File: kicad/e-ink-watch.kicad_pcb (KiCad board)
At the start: 4 copper layers, 40 x 40 mm, 45 parts, among them Q1 DMG2305UX, SW1 BTN1, SW2 BTN2, SW3 BTN3, U1 MDBT50Q-1MV2, U2 BQ25619, U3 MCP1700-3302

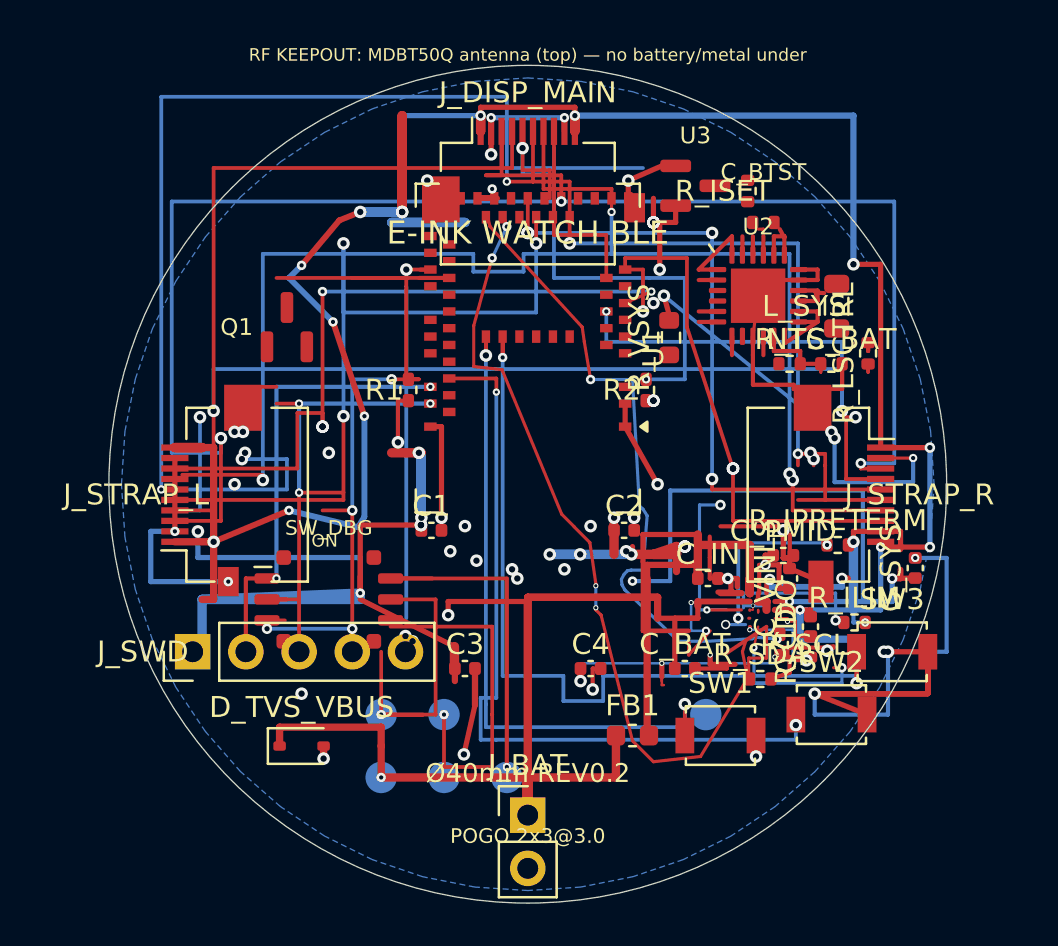
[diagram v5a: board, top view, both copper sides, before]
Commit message: Pass-BH: route VSYS, PSEL, and the display switch.
Unconnected drops from 22 to 17 with shorting_items still 0. The REGN path that failed clearance was not kept.

Co-authored-by: illiapliukhin <illiapliukhin@users.noreply.github.com>
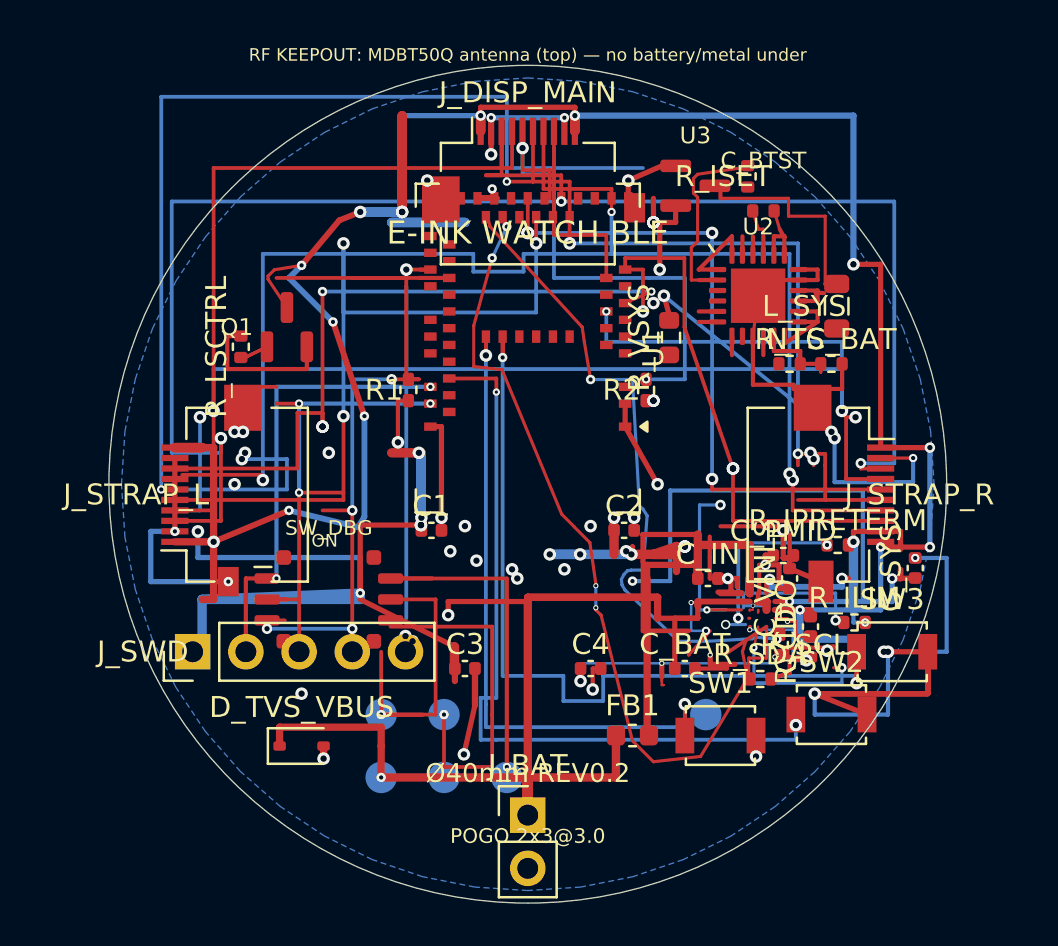
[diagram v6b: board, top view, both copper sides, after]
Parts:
- moved R_LSCTRL 30.0 mm to (86.3, 93.4)
- moved R_ISET 0.70 mm to (110.5, 85.3)
- moved C_BTST 0.55 mm to (111.2, 87.0)
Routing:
- net VSYS: track 32.4 -> 42.6 mm
- net PSEL: track 0.90 -> 9.01 mm
- net 3V3: track 105.3 -> 111.1 mm
- net 3V3_DISP: track 129.5 -> 133.0 mm
- net DISP_EN: track 0.80 -> 2.33 mm
- net BTST: track 1.48 -> 2.39 mm
- net SW: track 8.10 -> 9.01 mm
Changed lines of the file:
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@@
 	(footprint "R_0402_1005Metric"
 		(layer "F.Cu")
-		(at 110.5 86 90)
+		(at 110.5 85.3 90)
 		(descr "Resistor SMD 0402 (1005 Metric), square (rectangular) end terminal, IPC-7351 nominal, (Body size source: IPC-SM-782 page 72, https://www.pcb-3d.com/wordpress/wp-content/uploads/ipc-sm-782a_amendment_1_and_2.pdf), generated with kicad-footprint-generator")
 		(tags "resistor")
@@
 	(footprint "R_0402_1005Metric"
 		(layer "F.Cu")
-		(at 116.25 93.75 90)
+		(at 86.3 93.438 90)
 		(descr "Resistor SMD 0402 (1005 Metric), square (rectangular) end terminal, IPC-7351 nominal, (Body size source: IPC-SM-782 page 72, https://www.pcb-3d.com/wordpress/wp-content/uploads/ipc-sm-782a_amendment_1_and_2.pdf), generated with kicad-footprint-generator")
 		(tags "resistor")
@@
 	(segment
 		(start 104.65 89.2)
-		(end 107.6 89.2)
+		(end 107.48 89.2)
 		(width 0.18)
 		(layer "F.Cu")
@@
 	)
 	(segment
-		(start 107.6 89.2)
-		(end 107.6 92.5)
+		(start 107.48 89.2)
+		(end 107.48 92.5)
 		(width 0.18)
 		(layer "F.Cu")
@@
 	)
 	(segment
-		(start 107.6 92.5)
+		(start 107.48 92.5)
 		(end 109.8 99.25)
 		(width 0.18)
@@
 	(footprint "Resistor_SMD:R_0402_1005Metric"
 		(layer "F.Cu")
-		(at 111.25 87.5)
+		(at 111.25 86.95)
 		(descr "47nF")
 		(property "Reference" "C_BTST"
@@
 	)
 	(segment
-		(start 116.25 94.26)
-		(end 116.25 94.66)
+		(start 86.5 93.948)
+		(end 87.55 93.438)
 		(width 0.15)
 		(layer "F.Cu")
@@
 	)
 	(segment
-		(start 116.25 94.66)
-		(end 116.25 94.26)
+		(start 86.5 93.948)
+		(end 87.55 93.438)
 		(width 0.15)
 		(layer "F.Cu")
@@
 	)
 	(segment
-		(start 116.25 93.24)
-		(end 116.25 93.64)
+		(start 86.2 92.928)
+		(end 85.65 92.928)
 		(width 0.2)
 		(layer "F.Cu")
@@
 	)
 	(segment
-		(start 116.25 93.64)
-		(end 116.25 93.24)
+		(start 85.65 92.928)
+		(end 85.65 94.5)
 		(width 0.2)
 		(layer "F.Cu")
@@
 		(net 4)
 	)
+	(segment
+		(start 109.2 85.75)
+		(end 109.2 86.35)
+		(width 0.2)
+		(layer "F.Cu")
+		(net 5)
+	)
+	(segment
+		(start 109.2 86.35)
+		(end 112.45 86.35)
+		(width 0.15)
+		(layer "F.Cu")
+		(net 5)
+	)
+	(segment
+		(start 112.45 86.35)
+		(end 112.45 87.2)
+		(width 0.15)
+		(layer "F.Cu")
+		(net 5)
+	)
+	(segment
+		(start 112.45 87.2)
+		(end 114.2 87.2)
+		(width 0.15)
+		(layer "F.Cu")
+		(net 5)
+	)
+	(segment
+		(start 114.2 87.2)
+		(end 114.2 90.44)
+		(width 0.15)
+		(layer "F.Cu")
+		(net 5)
+	)
+	(segment
+		(start 114.2 90.44)
+		(end 114.75 90.438)
+		(width 0.2)
+		(layer "F.Cu")
+		(net 5)
+	)
+	(segment
+		(start 111.01 87.82)
+		(end 110.74 86.95)
+		(width 0.15)
+		(layer "F.Cu")
+		(net 40)
+	)
+	(segment
+		(start 112.03 87.82)
+		(end 111.76 86.95)
+		(width 0.15)
+		(layer "F.Cu")
+		(net 33)
+	)
+	(segment
+		(start 108.162 90.25)
+		(end 107.81 90.25)
+		(width 0.15)
+		(layer "F.Cu")
+		(net 39)
+	)
+	(segment
+		(start 107.81 90.25)
+		(end 107.81 88.7)
+		(width 0.15)
+		(layer "F.Cu")
+		(net 39)
+	)
+	(segment
+		(start 107.81 88.7)
+		(end 108.11 88.4)
+		(width 0.15)
+		(layer "F.Cu")
+		(net 39)
+	)
+	(segment
+		(start 108.11 88.4)
+		(end 108.11 86.3)
+		(width 0.15)
+		(layer "F.Cu")
+		(net 39)
+	)
+	(segment
+		(start 108.11 86.3)
+		(end 107.91 86.1)
+		(width 0.15)
+		(layer "F.Cu")
+		(net 39)
+	)
+	(segment
+		(start 107.91 86.1)
+		(end 107.91 85.4)
+		(width 0.15)
+		(layer "F.Cu")
+		(net 39)
+	)
+	(segment
+		(start 107.91 85.4)
+		(end 108.11 85.2)
+		(width 0.15)
+		(layer "F.Cu")
+		(net 39)
+	)
+	(segment
+		(start 108.11 85.2)
+		(end 110.5 84.85)
+		(width 0.15)
+		(layer "F.Cu")
+		(net 39)
+	)
+	(segment
+		(start 88.5 91.56)
+		(end 87.6 90.21)
+		(width 0.15)
+		(layer "F.Cu")
+		(net 3)
+	)
+	(segment
+		(start 87.6 90.21)
+		(end 87.6 90.06)
+		(width 0.15)
+		(layer "F.Cu")
+		(net 3)
+	)
+	(segment
+		(start 87.6 90.06)
+		(end 87.9 89.76)
+		(width 0.15)
+		(layer "F.Cu")
+		(net 3)
+	)
+	(segment
+		(start 87.9 89.76)
+		(end 89.2 89.55)
+		(width 0.15)
+		(layer "F.Cu")
+		(net 3)
+	)
+	(segment
+		(start 85.65 94.5)
+		(end 89.45 94.5)
+		(width 0.2)
+		(layer "F.Cu")
+		(net 2)
+	)
+	(segment
+		(start 89.45 94.5)
+		(end 89.45 93.8)
+		(width 0.2)
+		(layer "F.Cu")
+		(net 2)
+	)
 	(via

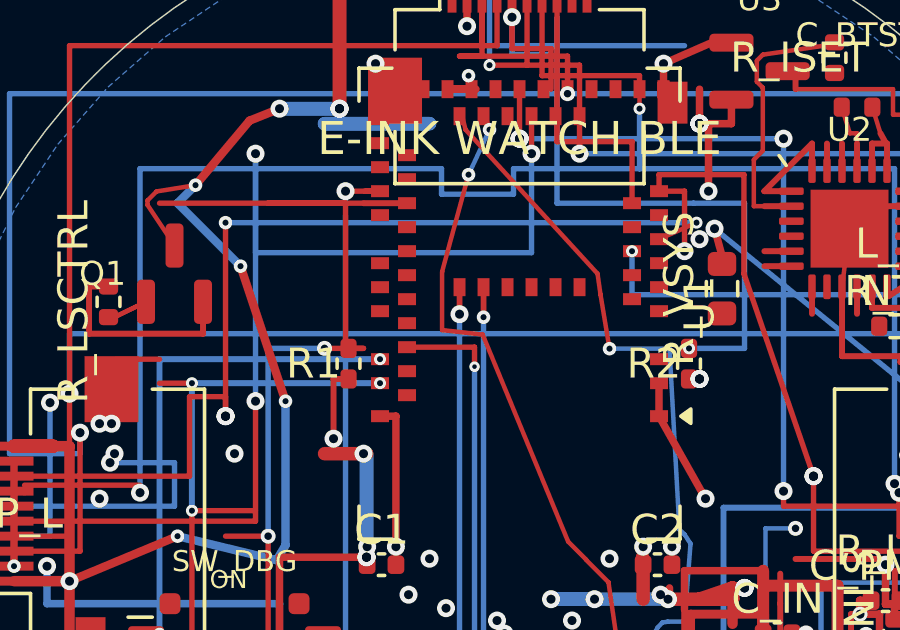
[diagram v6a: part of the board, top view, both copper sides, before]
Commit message: Pass-BI: join Q1 source to the module 3V3 rail.
Slide the EPD_BUSY_L via to (90.20, 90.96) so one 0.15 mm track fits under nRESET, and land that track on the module rail at (93.80, 96.30). shorting stays 0, unc 17 to 16.

Co-authored-by: illiapliukhin <illiapliukhin@users.noreply.github.com>
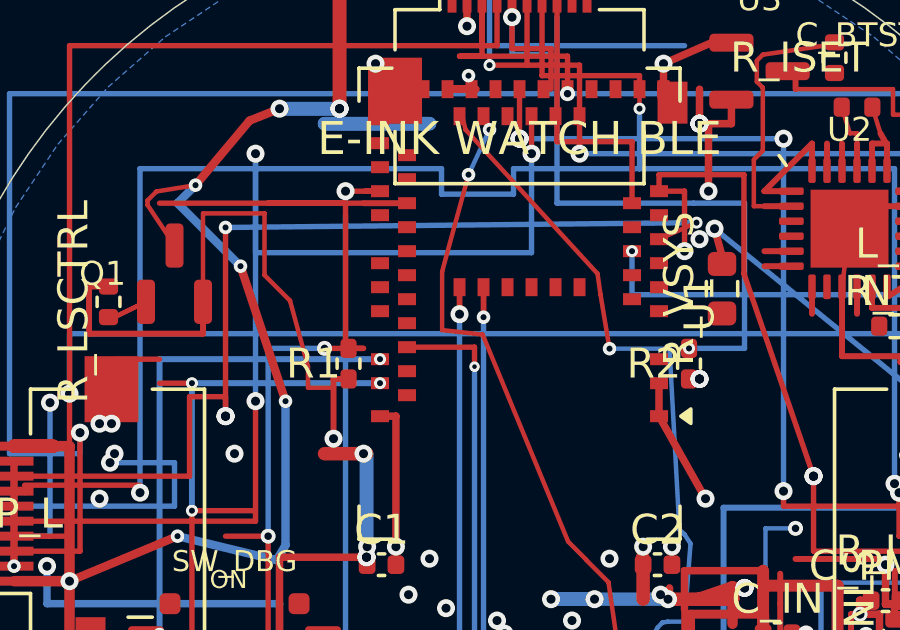
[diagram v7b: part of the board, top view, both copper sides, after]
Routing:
- net 3V3: track 111.1 -> 123.5 mm
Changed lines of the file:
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@@
 	(segment
 		(start 105.9 90.8)
-		(end 90.2 90.8)
+		(end 90.2 90.96)
 		(width 0.18)
 		(layer "B.Cu")
@@
 	)
 	(via
-		(at 90.2 90.8)
+		(at 90.2 90.96)
 		(size 0.45)
 		(drill 0.2)
@@
 	)
 	(segment
-		(start 90.2 90.8)
+		(start 90.2 90.96)
 		(end 90.2 97.25)
 		(width 0.18)
@@
 		(layer "F.Cu")
 		(net 2)
+	)
+	(segment
+		(start 89.45 93.8)
+		(end 89.45 90.49)
+		(width 0.15)
+		(layer "F.Cu")
+		(net 2)
+	)
+	(segment
+		(start 89.45 90.49)
+		(end 91.5 90.49)
+		(width 0.15)
+		(layer "F.Cu")
+		(net 2)
+	)
+	(segment
+		(start 91.5 90.49)
+		(end 91.5 92.55)
+		(width 0.15)
+		(layer "F.Cu")
+		(net 2)
+	)
+	(segment
+		(start 91.5 92.55)
+		(end 92.35 93.4)
+		(width 0.15)
+		(layer "F.Cu")
+		(net 2)
+	)
+	(segment
+		(start 92.35 93.4)
+		(end 92.95 95.6)
+		(width 0.15)
+		(layer "F.Cu")
+		(net 2)
+	)
+	(segment
+		(start 92.95 95.6)
+		(end 92.95 96.3)
+		(width 0.15)
+		(layer "F.Cu")
+		(net 2)
+	)
+	(segment
+		(start 92.95 96.3)
+		(end 93.8 96.3)
+		(width 0.15)
+		(layer "F.Cu")
+		(net 2)
